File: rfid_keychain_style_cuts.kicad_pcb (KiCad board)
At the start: 2 copper layers, 34 x 37 mm, 0 parts

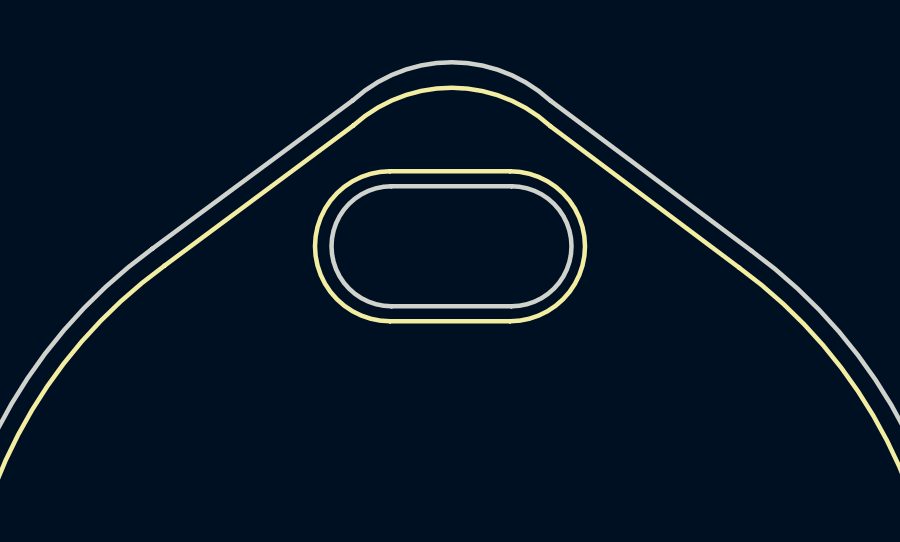
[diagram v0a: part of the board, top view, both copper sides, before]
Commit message: Tweaks for round inner hole style RFID tag
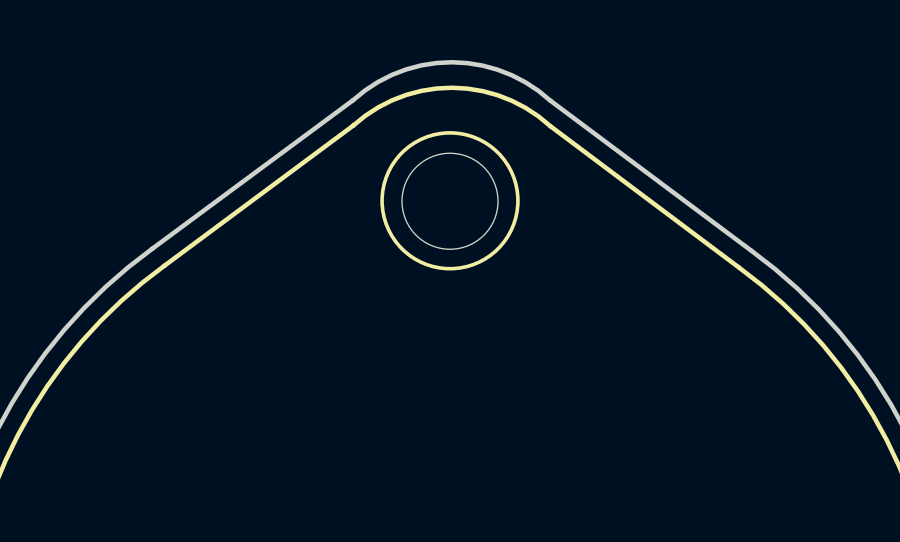
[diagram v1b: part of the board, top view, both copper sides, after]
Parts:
- added REF**: MountingHole_3.2mm_M3, MountingHole:MountingHole_3.2mm_M3, F.Cu at (107.8, 36.2)
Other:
- outline, holes or cut-outs redrawn
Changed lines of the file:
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@@
   (general
     (thickness 1.6)
-    (drawings 34)
+    (drawings 22)
     (tracks 0)
     (zones 0)
-    (modules 0)
+    (modules 1)
     (nets 1)
   )
@@
       (drillshape 0)
       (scaleselection 1)
-      (outputdirectory "GERBERS/rev1/"))
+      (outputdirectory "GERBERS/round_hole/"))
   )
   (net 0 "")
@@
     (uvia_drill 0.1)
   )
-  (gr_line (start 105.75 40.25) (end 109.75 40.25) (layer B.SilkS) (width 0.15))
-  (gr_arc (start 105.75 37.75) (end 105.75 35.25) (angle -180) (layer B.SilkS) (width 0.15))
-  (gr_arc (start 109.75 37.75) (end 109.75 40.25) (angle -180) (layer B.SilkS) (width 0.15))
-  (gr_line (start 105.75 35.25) (end 109.75 35.25) (layer F.SilkS) (width 0.15))
+  (module MountingHole:MountingHole_3.2mm_M3 (layer F.Cu)
+    (at 107.75 36.25)
+    (descr "Mounting Hole 3.2mm, no annular, M3")
+    (tags "mounting hole 3.2mm no annular m3")
+    (attr virtual)
+    (fp_text reference REF** (at 0 -4.2) (layer F.SilkS) hide
+      (effects (font (size 1 1) (thickness 0.15)))
+    )
+    (fp_text value MountingHole_3.2mm_M3 (at 0 4.2) (layer F.Fab)
+      (effects (font (size 1 1) (thickness 0.15)))
+    )
+    (fp_circle (center 0 0) (end 3.45 0) (layer F.CrtYd) (width 0.05))
+    (fp_circle (center 0 0) (end 3.2 0) (layer Cmts.User) (width 0.15))
+    (fp_text user %R (at 0.3 0) (layer F.Fab)
+      (effects (font (size 1 1) (thickness 0.15)))
+    )
+    (pad 1 np_thru_hole circle (at 0 0) (size 3.2 3.2) (drill 3.2) (layers *.Cu *.Mask))
+  )
+  (gr_circle (center 107.75 36.263846) (end 110.013846 36.263846) (layer B.SilkS) (width 0.12))
+  (gr_circle (center 107.75 36.234436) (end 105.5 36.484436) (layer F.SilkS) (width 0.12))
   (gr_line (start 117.388744 38.463985) (end 111.098342 33.748794) (layer F.SilkS) (width 0.15))
   (gr_arc (start 107.800001 51.649999) (end 124.103757 51.6) (angle -53.8) (layer F.SilkS) (width 0.15))
@@
   (gr_line (start 98.239928 38.393277) (end 104.520216 33.731574) (layer B.SilkS) (width 0.15))
   (gr_arc (start 107.800001 37.349999) (end 111.1 33.75) (angle -84.7) (layer B.SilkS) (width 0.15))
-  (gr_line (start 105.75 40.25) (end 109.75 40.25) (layer F.SilkS) (width 0.15))
-  (gr_line (start 105.75 35.25) (end 109.75 35.25) (layer B.SilkS) (width 0.15))
-  (gr_arc (start 109.75 37.75) (end 109.75 40.25) (angle -180) (layer F.SilkS) (width 0.15))
-  (gr_arc (start 105.75 37.75) (end 105.75 35.25) (angle -180) (layer F.SilkS) (width 0.15))
   (gr_line (start 117.390402 38.465191) (end 111.1 33.75) (layer B.SilkS) (width 0.15))
   (gr_line (start 98.239928 38.393277) (end 104.520216 33.731574) (layer F.SilkS) (width 0.15))
@@
   )
   (gr_arc (start 107.800001 36.499999) (end 111.1 32.9) (angle -84.7) (layer Edge.Cuts) (width 0.15))
-  (dimension 8 (width 0.15) (layer Dwgs.User)
-    (gr_text "8.000 mm" (at 107.8 31.7) (layer Dwgs.User)
-      (effects (font (size 1 1) (thickness 0.15)))
-    )
-    (feature1 (pts (xy 111.8 38) (xy 111.8 32.413579)))
-    (feature2 (pts (xy 103.8 38) (xy 103.8 32.413579)))
-    (crossbar (pts (xy 103.8 33) (xy 111.8 33)))
-    (arrow1a (pts (xy 111.8 33) (xy 110.673496 33.586421)))
-    (arrow1b (pts (xy 111.8 33) (xy 110.673496 32.413579)))
-    (arrow2a (pts (xy 103.8 33) (xy 104.926504 33.586421)))
-    (arrow2b (pts (xy 103.8 33) (xy 104.926504 32.413579)))
-  )
-  (gr_line (start 105.8 39.75) (end 109.8 39.75) (layer Edge.Cuts) (width 0.15))
-  (gr_arc (start 105.8 37.75) (end 105.8 35.75) (angle -180) (layer Edge.Cuts) (width 0.15))
-  (gr_line (start 105.8 35.75) (end 109.8 35.75) (layer Edge.Cuts) (width 0.15))
   (dimension 37 (width 0.15) (layer Dwgs.User)
     (gr_text "37.000 mm" (at 94.5 50.1 90) (layer Dwgs.User)
@@
     (arrow2b (pts (xy 95.8 68.6) (xy 95.213579 67.473496)))
   )
-  (gr_arc (start 109.8 37.75) (end 109.8 39.75) (angle -180) (layer Edge.Cuts) (width 0.15))
-  (dimension 4 (width 0.15) (layer Dwgs.User)
-    (gr_text "4.000 mm" (at 100.5 37.75 270) (layer Dwgs.User)
-      (effects (font (size 1 1) (thickness 0.15)))
-    )
-    (feature1 (pts (xy 105.8 39.75) (xy 101.213579 39.75)))
-    (feature2 (pts (xy 105.8 35.75) (xy 101.213579 35.75)))
-    (crossbar (pts (xy 101.8 35.75) (xy 101.8 39.75)))
-    (arrow1a (pts (xy 101.8 39.75) (xy 101.213579 38.623496)))
-    (arrow1b (pts (xy 101.8 39.75) (xy 102.386421 38.623496)))
-    (arrow2a (pts (xy 101.8 35.75) (xy 101.213579 36.876504)))
-    (arrow2b (pts (xy 101.8 35.75) (xy 102.386421 36.876504)))
-  )
   (gr_arc (start 107.800001 51.649999) (end 124.8 51.6) (angle -53.8041147) (layer Edge.Cuts) (width 0.15))
